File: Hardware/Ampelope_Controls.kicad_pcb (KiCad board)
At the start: 2 copper layers, 60.5 x 110 mm, 36 parts, among them J1 Conn_01x12_Male, J10 Audio2_In, J11 Audio3_In, J12 Audio4_In, J13 Audio1_Out, J14 Audio2_Out, J15 Audio3_Out, J16 Audio4_Out, J17 Clock_In, J18 Env1_Out, J19 Env3_Out, J2 Conn_01x12_Male, J3 Conn_01x12_Male, J4 Conn_01x12_Male, J5 Gate1_In, J6 Gate2_In, J7 Gate3_In, J8 Gate4_In, J9 Audio1_In

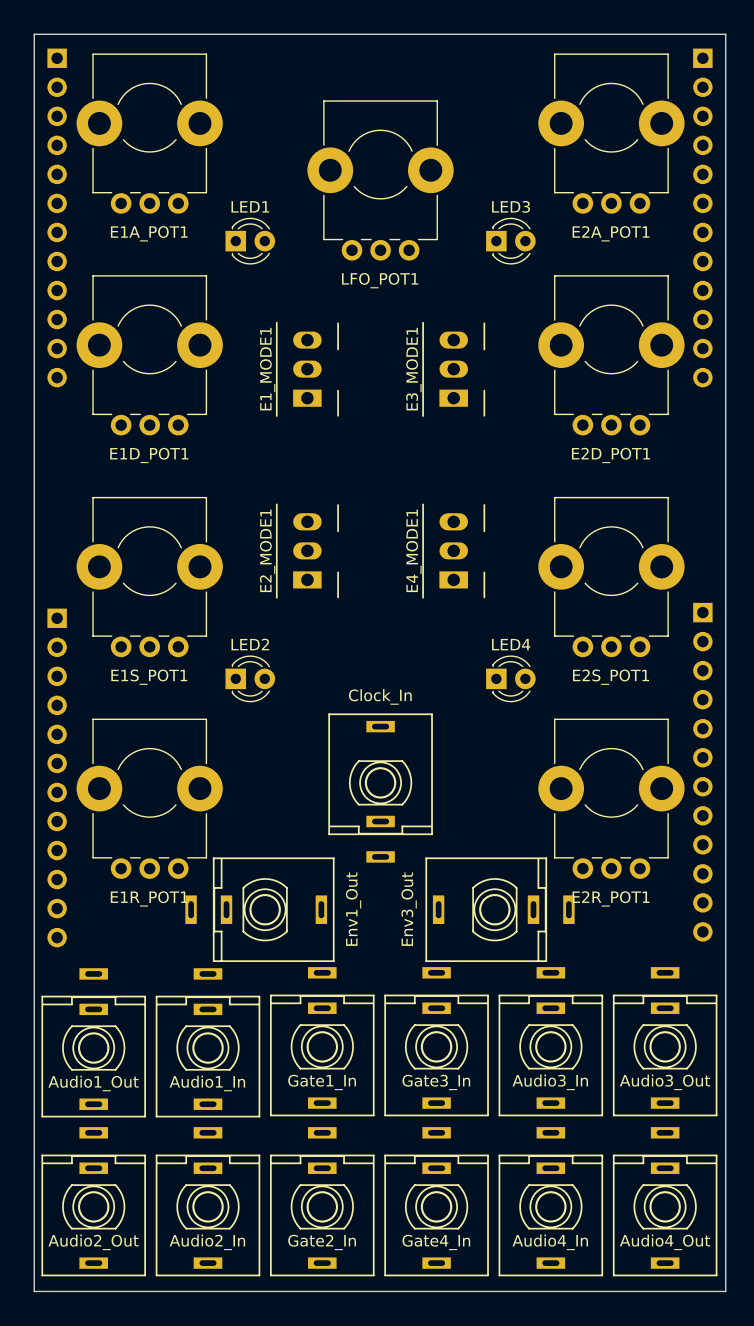
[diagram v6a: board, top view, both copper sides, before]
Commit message: Wired up control board
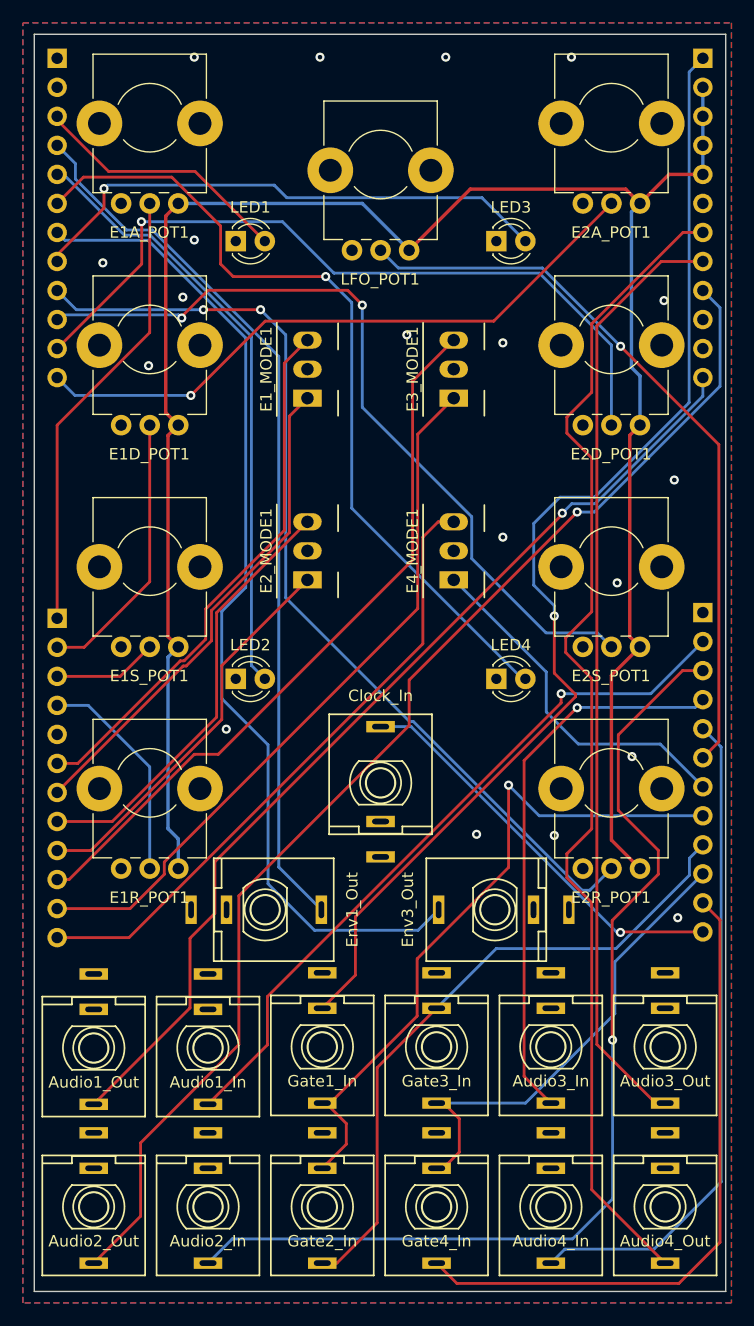
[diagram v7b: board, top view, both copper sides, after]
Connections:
- E1A_POT1 pad 1: +3.3VA -> +3V3
- E1D_POT1 pad 1: +3.3VA -> +3V3
- E1R_POT1 pad 1: +3.3VA -> +3V3
- E1S_POT1 pad 1: +3.3VA -> +3V3
- E2A_POT1 pad 1: +3.3VA -> +3V3
- E2D_POT1 pad 1: +3.3VA -> +3V3
- E2R_POT1 pad 1: +3.3VA -> +3V3
- E2S_POT1 pad 1: +3.3VA -> +3V3
- J1 pad 1: /Led1_Out -> /Gate_In
- J1 pad 10: /Env2_LFO -> GND
- J1 pad 11: unconnected-(J1-Pad11) -> GND
- J1 pad 12: unconnected-(J1-Pad12) -> /Audio1_Out
- J1 pad 2: /Env1_Out -> +3V3
- J1 pad 3: /Led2_Out -> +3V3
- J1 pad 4: /Env2_Out -> +3V3
- J1 pad 5: /Led3_Out -> +3V3
- J1 pad 6: /Env3_Out -> GND
- J1 pad 7: /Led4_Out -> /Audio4_Out
- J1 pad 8: /Env4_Out -> /Audio3_Out
- J1 pad 9: /Env2_Short -> /Audio2_Out
- J2 pad 1: /Audio1_Out -> GND
- J2 pad 10: /Env1_LFO -> /Gate3_In
- J2 pad 11: unconnected-(J2-Pad11) -> /Gate4_In
- J2 pad 12: unconnected-(J2-Pad12) -> /Clock_In
- J2 pad 2: /Audio2_Out -> /Audio1_In
- J2 pad 3: /Audio3_Out -> /Audio2_In
- J2 pad 4: /Audio4_Out -> /Audio3_In
- J2 pad 5: /Audio1_In -> /Audio4_In
- J2 pad 6: /Audio2_In -> /LFO_Speed
- J2 pad 7: /Audio3_In -> /Env4_Short
- J2 pad 8: /Audio4_In -> /Gate1_In
- J2 pad 9: /Env1_Short -> /Gate2_In
- J3 pad 1: /LFO_Speed -> GND
- J3 pad 10: /Clock_In -> /EnvB_Sustain
- J3 pad 11: unconnected-(J3-Pad11) -> /EnvB_Decay
- J3 pad 12: unconnected-(J3-Pad12) -> /EnvB_Attack
- J3 pad 2: /EnvB_Attack -> GND
- J3 pad 3: /EnvB_Decay -> /Led1_Out
- J3 pad 4: /EnvB_Sustain -> /Env1_Out
- J3 pad 5: /EnvB_Release -> /Led2_Out
- J3 pad 6: /Env3_Short -> /Led4_Out
- J3 pad 7: /Env3_LFO -> /Env3_Out
- J3 pad 8: /Env4_Short -> /Led3_Out
- J3 pad 9: /Env4_LFO -> /EnvB_Release
- J4 pad 1: /Gate1_In -> /EnvA_Attack
- J4 pad 10: unconnected-(J4-Pad10) -> /Env3_LFO
- J4 pad 11: unconnected-(J4-Pad11) -> /Env3_Short
- J4 pad 12: unconnected-(J4-Pad12) -> /Env4_LFO
- J4 pad 2: /Gate2_In -> /EnvA_Decay
- J4 pad 3: /Gate3_In -> /EnvA_Sustain
- J4 pad 4: /Gate4_In -> /EnvA_Release
- J4 pad 5: /EnvA_Attack -> GND
- J4 pad 6: /EnvA_Decay -> /Env1_LFO
- J4 pad 7: /EnvA_Sustain -> /Env1_Short
- J4 pad 8: /EnvA_Release -> /Env2_LFO
- J4 pad 9: unconnected-(J4-Pad9) -> /Env2_Short
- LFO_POT1 pad 1: +3.3VA -> +3V3
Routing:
- net +3V3: track 0.00 -> 181.2 mm
- net /Audio2_Out: track 0.00 -> 109.3 mm, vias 0 -> 1
- net /Audio4_Out: track 0.00 -> 103.4 mm
- net /Gate_In: track 0.00 -> 101.7 mm, vias 0 -> 1
- net /Audio2_In: track 0.00 -> 91.2 mm, vias 0 -> 1
- net /Env3_Out: track 0.00 -> 88.0 mm
- net /Audio1_Out: track 0.00 -> 86.5 mm, vias 0 -> 1
- net /EnvB_Release: track 0.00 -> 84.5 mm, vias 0 -> 2
- net /Audio3_Out: track 0.00 -> 82.6 mm
- net /Env1_Out: track 0.00 -> 77.8 mm
- net /Led4_Out: track 0.00 -> 72.3 mm, vias 0 -> 1
- net /EnvB_Sustain: track 0.00 -> 70.2 mm, vias 0 -> 2
- net /EnvB_Decay: track 0.00 -> 66.8 mm, vias 0 -> 1
- net /LFO_Speed: track 0.00 -> 64.6 mm, vias 0 -> 1
- net /Env3_LFO: track 0.00 -> 63.4 mm
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- added copper zone on B.Cu, net GND
- added copper zone on F.Cu, net GND

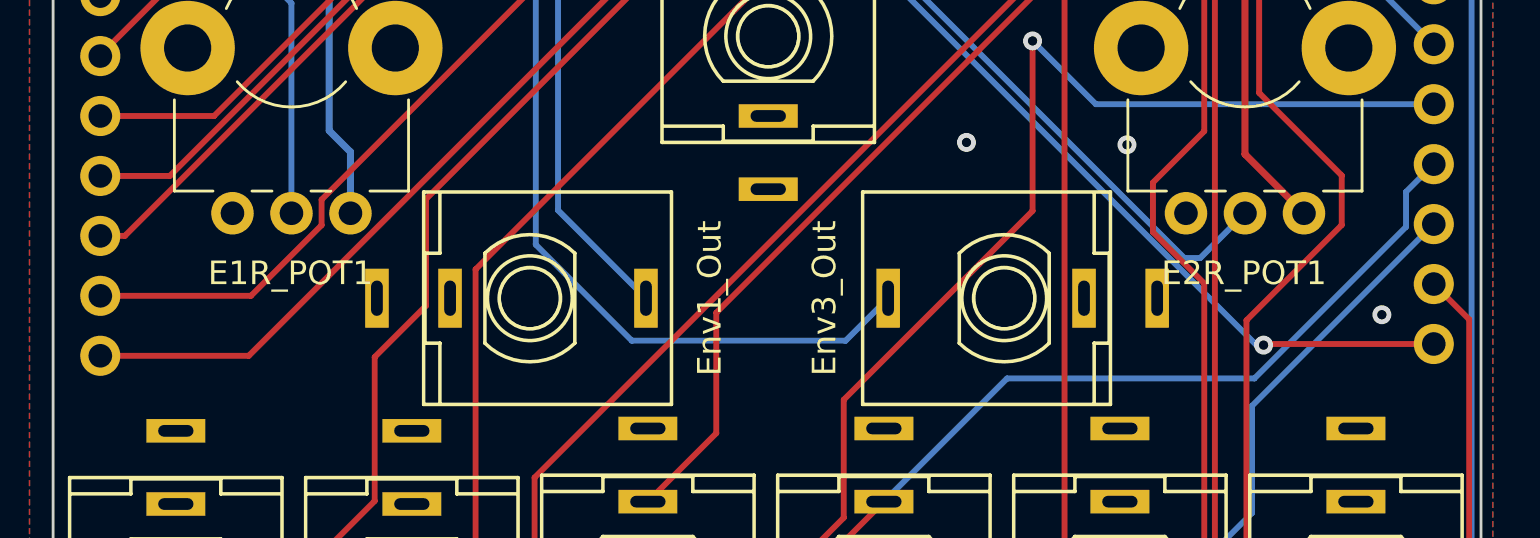
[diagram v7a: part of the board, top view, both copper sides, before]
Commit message: Fixed DRC errors on control and component boards
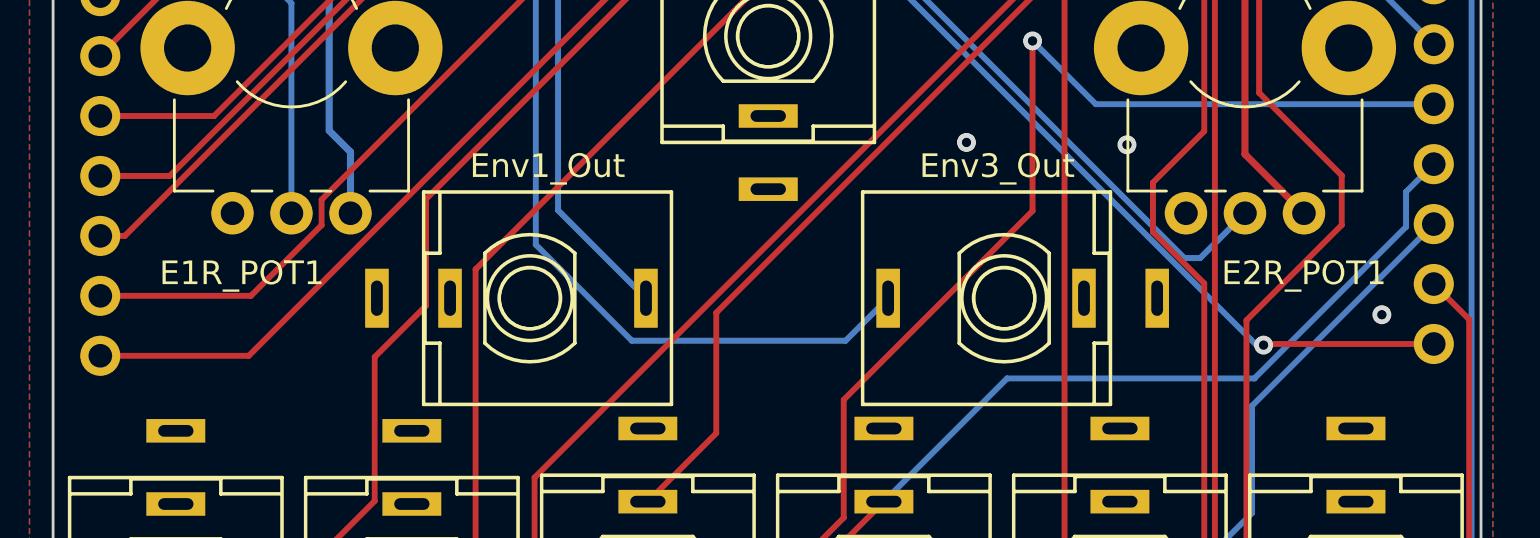
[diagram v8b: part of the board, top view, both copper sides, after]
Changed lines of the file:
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@@
     (property "Sheetname" "")
     (attr through_hole)
-    (fp_text reference "E2R_POT1" (at -0.04 10.04) (layer "F.SilkS")
+    (fp_text reference "E2R_POT1" (at 2.5 10.04) (layer "F.SilkS")
       (effects (font (size 1 1) (thickness 0.15)))
     )
@@
       (effects (font (size 1 1) (thickness 0.15)))
     )
-    (fp_text value "Env1_Out" (at 0 -7.62 90) (layer "F.SilkS")
+    (fp_text value "Env1_Out" (at -5.6 -0.75 180) (layer "F.SilkS")
       (effects (font (size 1 1) (thickness 0.15)))
     )
@@
       (effects (font (size 1 1) (thickness 0.15)))
     )
-    (fp_text value "Env3_Out" (at 0 -7.62 90) (layer "F.SilkS")
+    (fp_text value "Env3_Out" (at 5.6 -0.3 180) (layer "F.SilkS")
       (effects (font (size 1 1) (thickness 0.15)))
     )
@@
       (effects (font (size 1 1) (thickness 0.15)))
     )
-    (fp_line (start -4.961 6.56) (end -4.961 2.694) (layer "F.SilkS") (width 0.12))
+    (fp_line (start -4.961 -1.695) (end -4.961 -5.56) (layer "F.SilkS") (width 0.12))
+    (fp_line (start 4.96 6.56) (end 4.96 2.694) (layer "F.SilkS") (width 0.12))
     (fp_line (start 0.825 6.56) (end 1.675 6.56) (layer "F.SilkS") (width 0.12))
-    (fp_line (start -1.675 6.56) (end -0.825 6.56) (layer "F.SilkS") (width 0.12))
-    (fp_line (start 3.325 6.56) (end 4.96 6.56) (layer "F.SilkS") (width 0.12))
-    (fp_line (start -4.961 -1.695) (end -4.961 -5.56) (layer "F.SilkS") (width 0.12))
-    (fp_line (start 4.96 -1.695) (end 4.96 -5.56) (layer "F.SilkS") (width 0.12))
-    (fp_line (start 4.96 6.56) (end 4.96 2.694) (layer "F.SilkS") (width 0.12))
     (fp_line (start -4.961 6.56) (end -3.325 6.56) (layer "F.SilkS") (width 0.12))
     (fp_line (start -4.961 -5.56) (end 4.96 -5.56) (layer "F.SilkS") (width 0.12))
+    (fp_line (start -1.675 6.56) (end -0.825 6.56) (layer "F.SilkS") (width 0.12))
+    (fp_line (start 4.96 -1.695) (end 4.96 -5.56) (layer "F.SilkS") (width 0.12))
+    (fp_line (start -4.961 6.56) (end -4.961 2.694) (layer "F.SilkS") (width 0.12))
+    (fp_line (start 3.325 6.56) (end 4.96 6.56) (layer "F.SilkS") (width 0.12))
     (fp_arc (start 0 0) (end 2.762 -1.173) (angle -134) (layer "F.SilkS") (width 0.12))
     (fp_arc (start 0 0) (end -2.298 1.928) (angle -100) (layer "F.SilkS") (width 0.12))
     (fp_line (start 0.2 0) (end -0.2 0) (layer "Dwgs.User") (width 0.01))
     (fp_line (start 0 0.19) (end 0 -0.21) (layer "Dwgs.User") (width 0.01))
-    (fp_line (start -6.65 -5.75) (end -6.65 8.65) (layer "F.CrtYd") (width 0.05))
-    (fp_line (start -6.65 8.65) (end 6.65 8.65) (layer "F.CrtYd") (width 0.05))
     (fp_line (start 6.65 8.65) (end 6.65 -5.75) (layer "F.CrtYd") (width 0.05))
     (fp_line (start 6.65 -5.75) (end -6.65 -5.75) (layer "F.CrtYd") (width 0.05))
+    (fp_line (start -6.65 8.65) (end 6.65 8.65) (layer "F.CrtYd") (width 0.05))
+    (fp_line (start -6.65 -5.75) (end -6.65 8.65) (layer "F.CrtYd") (width 0.05))
     (fp_line (start 4.9 6.5) (end 4.9 -5.5) (layer "F.Fab") (width 0.1))
+    (fp_line (start -4.9 -5.5) (end -4.9 6.5) (layer "F.Fab") (width 0.1))
+    (fp_line (start -4.9 6.5) (end 4.9 6.5) (layer "F.Fab") (width 0.1))
     (fp_line (start 4.9 -5.5) (end -4.9 -5.5) (layer "F.Fab") (width 0.1))
-    (fp_line (start -4.9 6.5) (end 4.9 6.5) (layer "F.Fab") (width 0.1))
-    (fp_line (start -4.9 -5.5) (end -4.9 6.5) (layer "F.Fab") (width 0.1))
     (fp_circle (center 0 0) (end 0 -3.25) (layer "F.Fab") (width 0.1) (fill none))
     (fp_circle (center 0 0) (end 0 -3) (layer "F.Fab") (width 0.1) (fill none))
+    (pad "0" np_thru_hole circle locked (at 4.4 0.5 90) (size 4 4) (drill 2) (layers *.Cu *.Mask))
     (pad "0" np_thru_hole circle locked (at -4.4 0.5 90) (size 4 4) (drill 2) (layers *.Cu *.Mask))
-    (pad "0" np_thru_hole circle locked (at 4.4 0.5 90) (size 4 4) (drill 2) (layers *.Cu *.Mask))
     (pad "1" thru_hole circle locked (at 2.5 7.5 90) (size 1.8 1.8) (drill 1) (layers *.Cu *.Mask)
-      (net 15 "+3V3") (pinfunction "1") (pintype "passive"))
+      (net 15 "+3V3") (pinfunction "1"))
     (pad "2" thru_hole circle locked (at 0 7.5 90) (size 1.8 1.8) (drill 1) (layers *.Cu *.Mask)
-      (net 26 "/LFO_Speed") (pinfunction "2") (pintype "passive"))
+      (net 26 "/LFO_Speed") (pinfunction "2"))
     (pad "3" thru_hole circle locked (at -2.5 7.5 90) (size 1.8 1.8) (drill 1) (layers *.Cu *.Mask)
-      (net 1 "GND") (pinfunction "3") (pintype "passive"))
+      (net 1 "GND") (pinfunction "3"))
     (model "D:/docs/kiCad/Custom_Footprints.pretty/3dmodels/ALPHA-RD901F-40.step"
       (offset (xyz -0 -0.2 0))
@@
     (property "Sheetname" "")
     (attr through_hole)
-    (fp_text reference "E1R_POT1" (at -0.04 10.04) (layer "F.SilkS")
-      (effects (font (size 1 1) (thickness 0.15)))
-    )
+    (fp_text reference "E1R_POT1" (at -2.1 10.04) (layer "F.SilkS")
+      (effects (font (size 1 1) (thickness 0.15)))
+    )
